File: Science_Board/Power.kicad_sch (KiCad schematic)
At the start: 29 parts, among them IC1 TCKE602RM, IC2 TCKE602RM, IC3 TCKE602RM, J21 Molex_Megafit_02, J3 Molex_Megafit_02, J4 Molex_Megafit_02, Q1 BS250, U1 AP63205WU

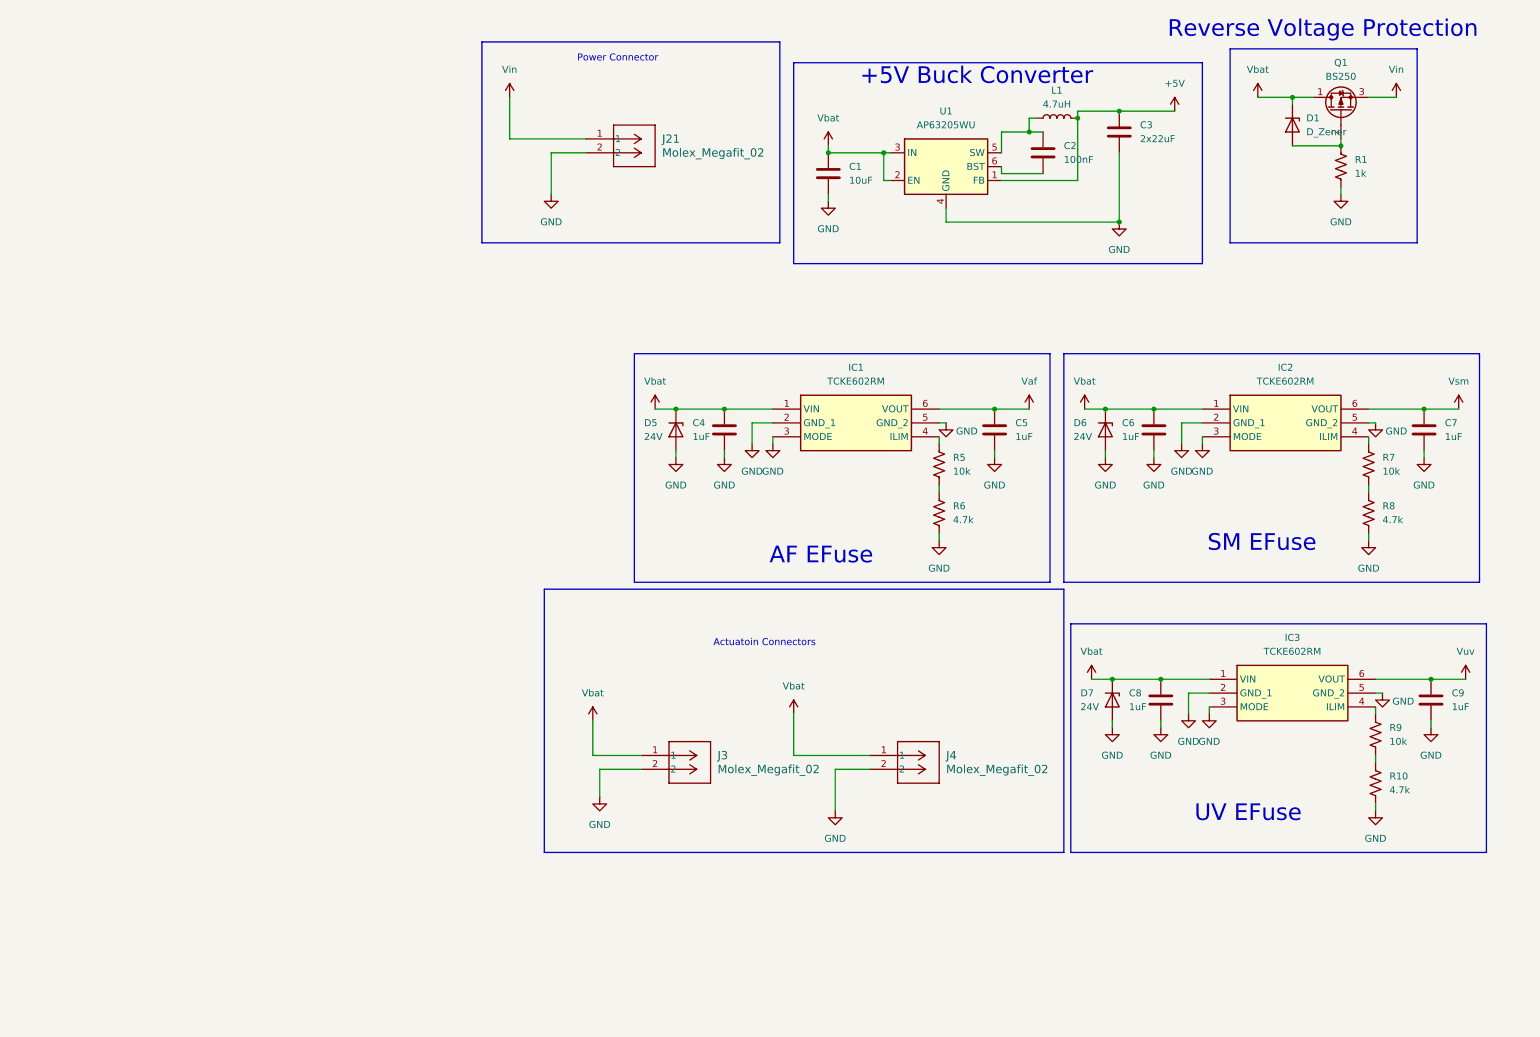
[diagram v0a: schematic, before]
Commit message: fuse trip
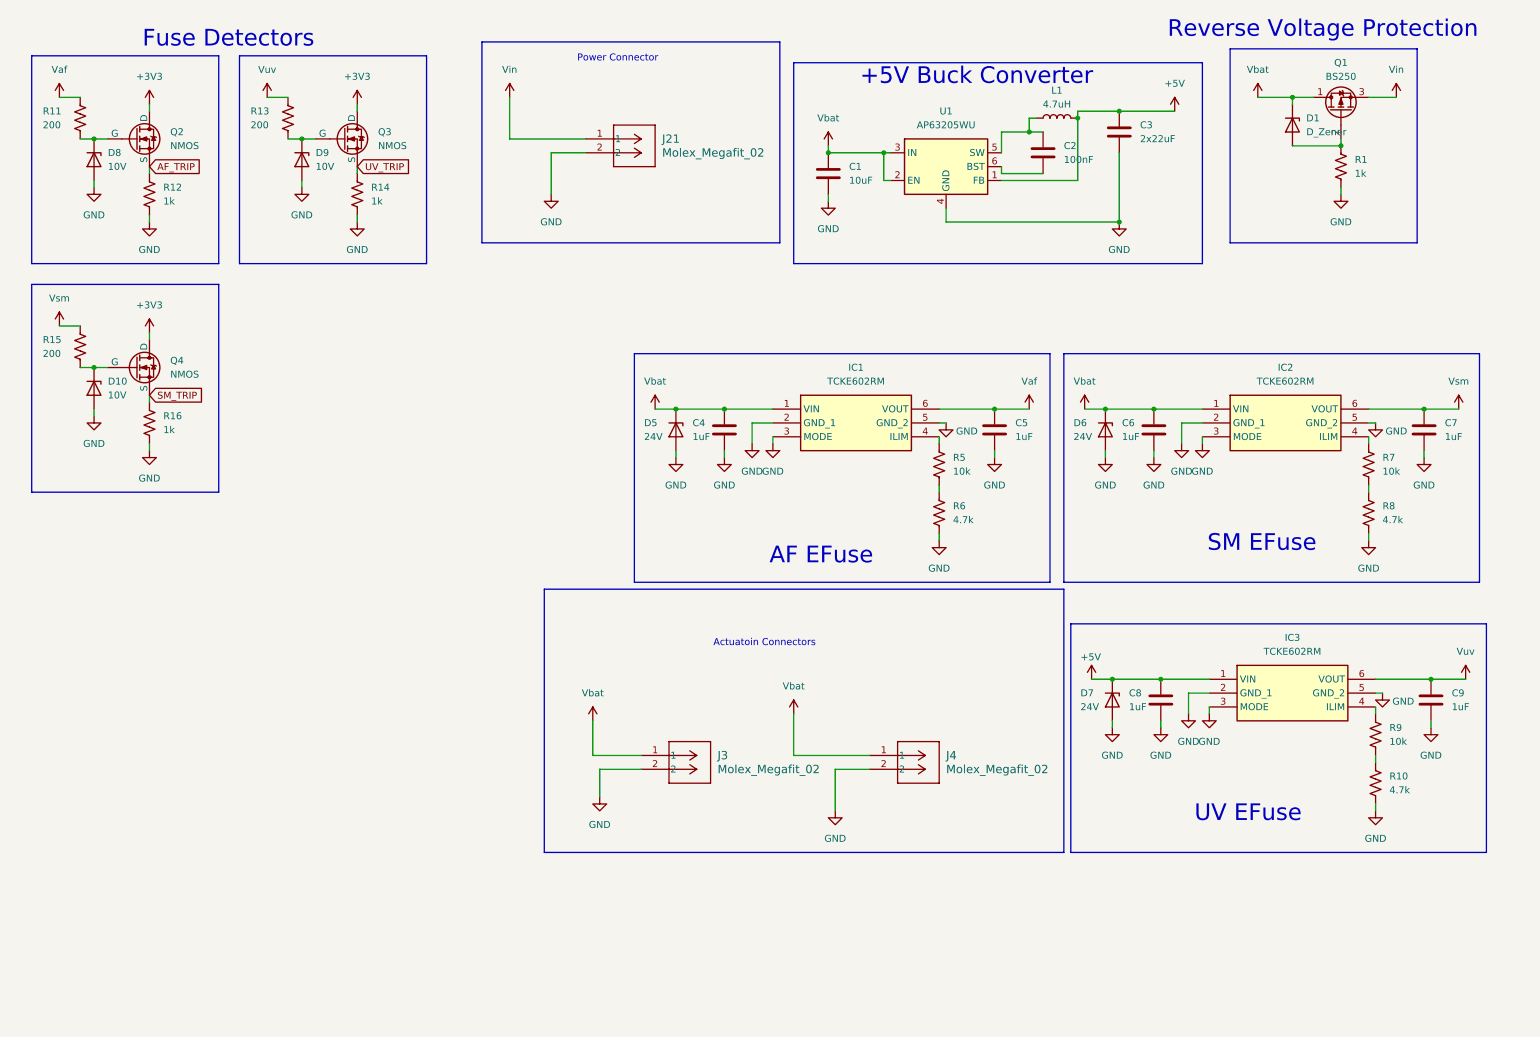
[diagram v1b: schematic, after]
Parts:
- added D10, D8, D9: 10V, Package_DIP:DIP-40_W15.24mm, symbol Device:D_Zener
- added Q2, Q3, Q4: NMOS, Package_DFN_QFN:Nordic_AQFN-94-1EP_7x7mm_P0.4mm, symbol Simulation_SPICE:NMOS
- added R11, R13, R15: 200, Resistor_SMD:R_0603_1608Metric_Pad0.98x0.95mm_HandSolder, symbol Device:R_US
- added R12, R14, R16: 1k, Resistor_SMD:R_0603_1608Metric_Pad0.98x0.95mm_HandSolder, symbol Device:R_US
- C4, C5, C6, C7, C8, C9: footprint (none) -> Capacitor_SMD:C_0603_1608Metric_Pad1.08x0.95mm_HandSolder
- IC1, IC2, IC3: footprint TCKE602RM -> MRDT_Devices:TCKE602RM
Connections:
- net +5V: now also C8.1, D7.1 (K), IC3.1 (VIN)
- net GND: now also D10.2 (A), D8.2 (A), D9.2 (A), R12.2, R14.2, R16.2
- net Vaf: now also R11.1
- net Vbat: no longer C8.1, D7.1 (K), IC3.1 (VIN)
- net Vsm: now also R15.1
- net Vuv: now also R13.1
- new net: D9.1 (K), Q3.2 (G), R13.2
- new net: D10.1 (K), Q4.2 (G), R15.2
- new net: D8.1 (K), Q2.2 (G), R11.2
- new net +3V3: Q2.1 (D), Q3.1 (D), Q4.1 (D)
- new net AF_TRIP: Q2.3 (S), R12.1
- new net SM_TRIP: Q4.3 (S), R16.1
- new net UV_TRIP: Q3.3 (S), R14.1
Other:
- note added: "Fuse Detectors"

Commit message: Add Footprints
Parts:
- R5, R7, R9: footprint (none) -> Resistor_SMD:R_0603_1608Metric
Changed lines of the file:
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@@
 			)
 		)
-		(property "Footprint" ""
+		(property "Footprint" "Resistor_SMD:R_0603_1608Metric"
 			(at 183.896 95.504 90)
 			(hide yes)
@@
 			)
 		)
-		(property "Footprint" ""
+		(property "Footprint" "Resistor_SMD:R_0603_1608Metric"
 			(at 262.636 95.504 90)
 			(hide yes)
@@
 			)
 		)
-		(property "Footprint" ""
+		(property "Footprint" "Resistor_SMD:R_0603_1608Metric"
 			(at 263.906 145.034 90)
 			(hide yes)

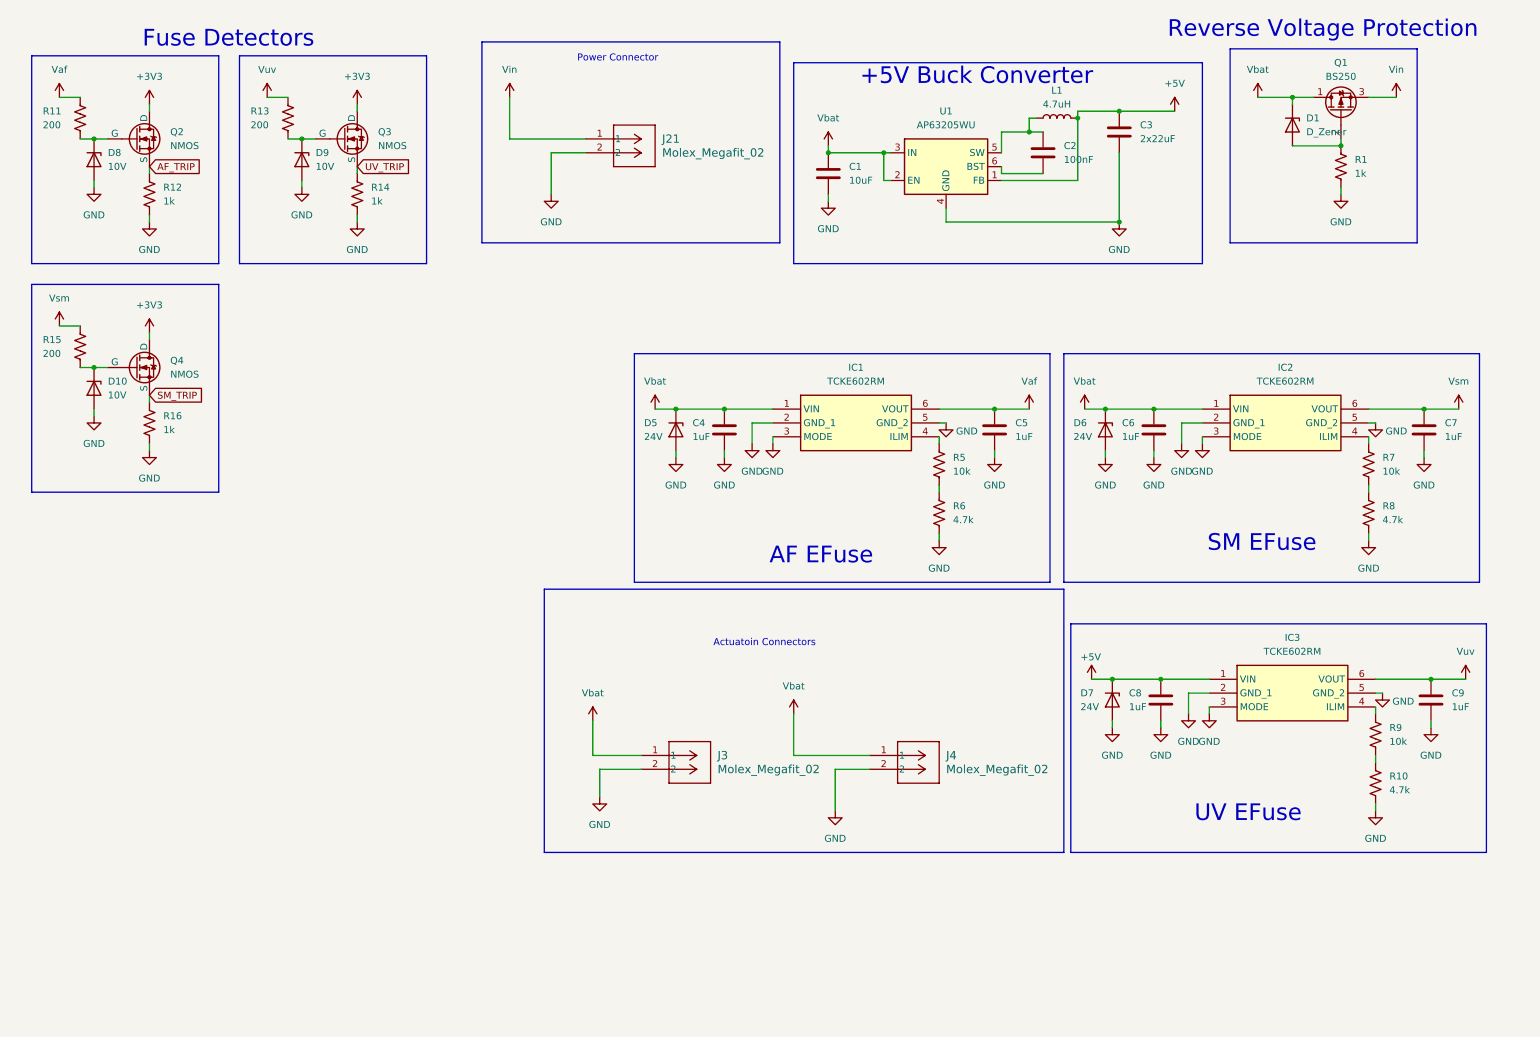
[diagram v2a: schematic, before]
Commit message: Fixed Reverse Voltage Protection, small formatting fixes
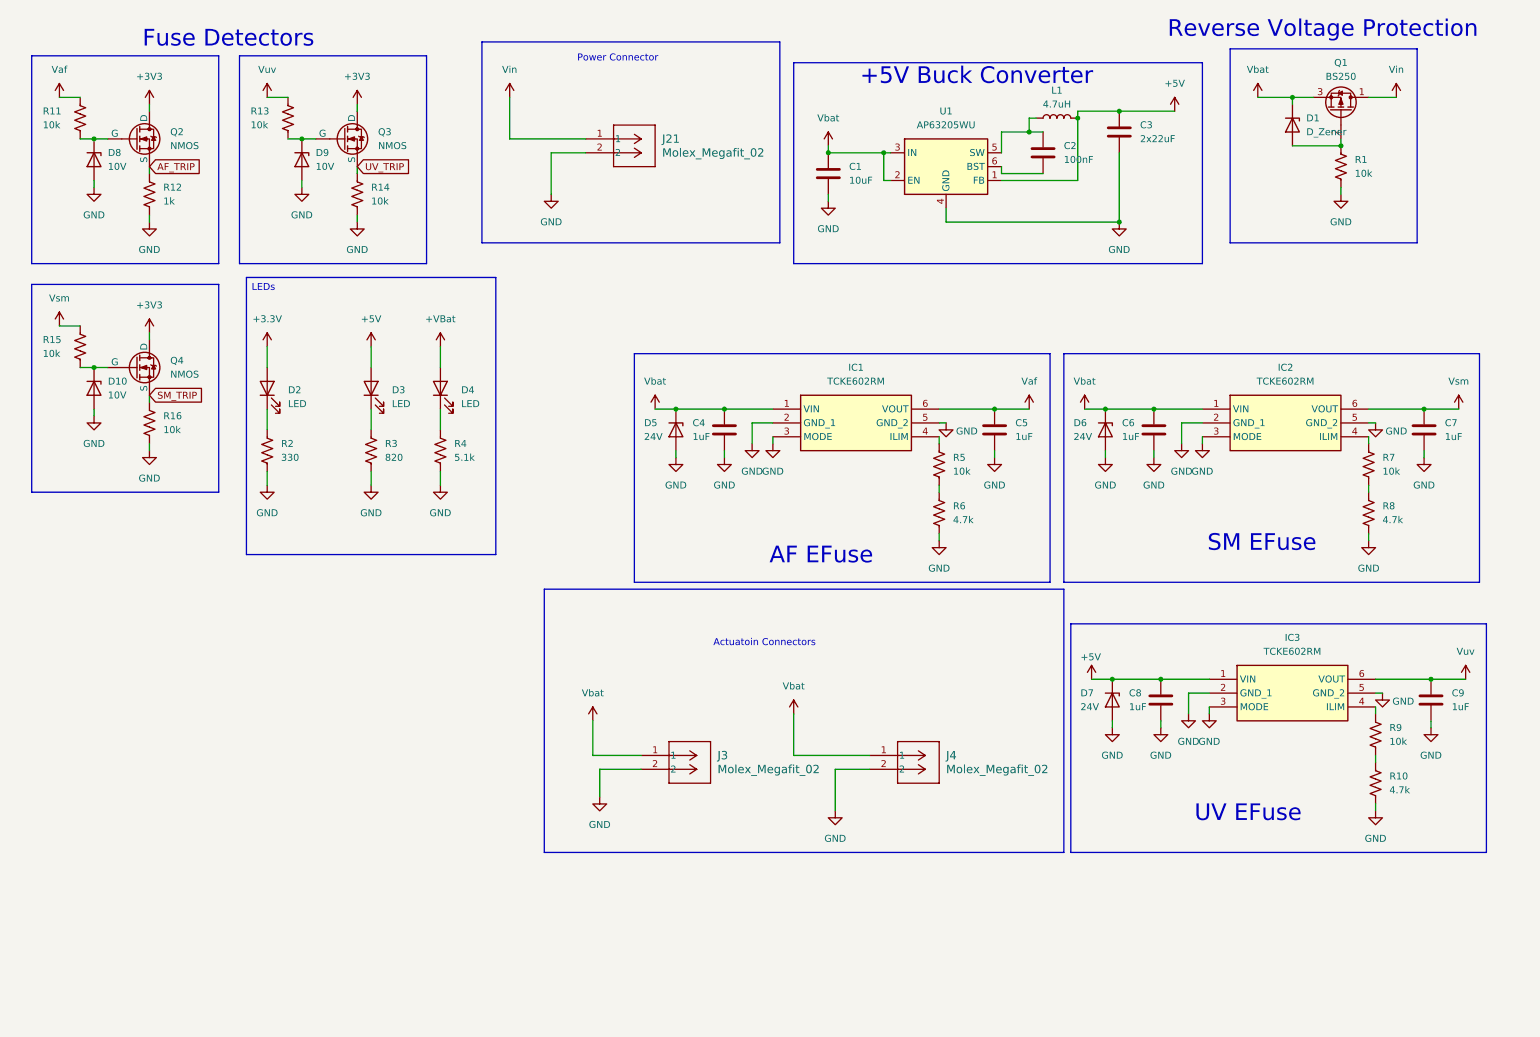
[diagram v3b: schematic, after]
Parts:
- added D2, D3, D4: LED, Diode_SMD:D_0603_1608Metric_Pad1.05x0.95mm_HandSolder, symbol Device:LED
- added R2: 330, Package_DIP:DIP-8_W7.62mm, symbol Device:R_US
- added R3: 820, Package_DIP:DIP-8_W7.62mm, symbol Device:R_US
- added R4: 5.1k, Package_DIP:DIP-8_W7.62mm, symbol Device:R_US
- R1, R14, R16: value 1k -> 10k
- R11, R13, R15: value 200 -> 10k
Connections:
- net +5V: now also D3.2 (A)
- net GND: now also R2.2, R3.2, R4.2
- net Vbat: now also Q1.3 (S); no longer Q1.1 (D)
- net Vin: now also Q1.1 (D); no longer Q1.3 (S)
- new net: D4.1 (K), R4.1
- new net: D3.1 (K), R3.1
- new net: D2.1 (K), R2.1
- new net +3.3V: D2.2 (A)
- new net +VBat: D4.2 (A)
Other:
- moved on the sheet: Q1

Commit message: Incorrect Efuse Package, fixed and added gpio connections for loadswitch functionality
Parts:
- IC1, IC2: value TCKE602RM -> TCKE603RA
- IC3: value TCKE602RM -> TCKE603RM
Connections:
- net GND: no longer IC1.3 (MODE), IC2.3 (MODE), IC3.3 (MODE)
- new net AF_EN: IC1.3 (EN)
- new net SM_EN: IC2.3 (EN)
- new net UV_EN: IC3.3 (EN)
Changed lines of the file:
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@@
 		)
 	)
+	(global_label "UV_EN"
+		(shape input)
+		(at 232.41 140.97 270)
+		(fields_autoplaced yes)
+		(effects
+			(font
+				(size 1.27 1.27)
+				(thickness 0.1588)
+			)
+			(justify right)
+		)
+		(property "Intersheetrefs" "${INTERSHEET_REFS}"
+			(at 232.41 149.8214 90)
+			(hide yes)
+			(show_name no)
+			(do_not_autoplace no)
+			(effects
+				(font
+					(size 1.27 1.27)
+				)
+				(justify right)
+			)
+		)
+	)
+	(global_label "AF_EN"
+		(shape input)
+		(at 152.4 91.44 270)
+		(fields_autoplaced yes)
+		(effects
+			(font
+				(size 1.27 1.27)
+				(thickness 0.1588)
+			)
+			(justify right)
+		)
+		(property "Intersheetrefs" "${INTERSHEET_REFS}"
+			(at 152.4 100.0495 90)
+			(hide yes)
+			(show_name no)
+			(do_not_autoplace no)
+			(effects
+				(font
+					(size 1.27 1.27)
+				)
+				(justify right)
+			)
+		)
+	)
+	(global_label "SM_EN"
+		(shape input)
+		(at 231.14 91.44 270)
+		(fields_autoplaced yes)
+		(effects
+			(font
+				(size 1.27 1.27)
+				(thickness 0.1588)
+			)
+			(justify right)
+		)
+		(property "Intersheetrefs" "${INTERSHEET_REFS}"
+			(at 231.14 100.5332 90)
+			(hide yes)
+			(show_name no)
+			(do_not_autoplace no)
+			(effects
+				(font
+					(size 1.27 1.27)
+				)
+				(justify right)
+			)
+		)
+	)
 	(global_label "AF_TRIP"
 		(shape input)
@@
 	)
 	(symbol
-		(lib_id "power:GND")
-		(at 232.41 140.97 0)
-		(unit 1)
-		(body_style 1)
-		(exclude_from_sim no)
-		(in_bom yes)
-		(on_board yes)
-		(in_pos_files yes)
-		(dnp no)
-		(fields_autoplaced yes)
-		(property "Reference" "#PWR038"
-			(at 232.41 147.32 0)
-			(hide yes)
-			(show_name no)
-			(do_not_autoplace no)
-			(effects
-				(font
-					(size 1.27 1.27)
-				)
-			)
-		)
-		(property "Value" "GND"
-			(at 232.41 146.05 0)
-			(show_name no)
-			(do_not_autoplace no)
-			(effects
-				(font
-					(size 1.27 1.27)
-				)
-			)
-		)
-		(property "Footprint" ""
-			(at 232.41 140.97 0)
-			(hide yes)
-			(show_name no)
-			(do_not_autoplace no)
-			(effects
-				(font
-					(size 1.27 1.27)
-				)
-			)
-		)
-		(property "Datasheet" ""
-			(at 232.41 140.97 0)
-			(hide yes)
-			(show_name no)
-			(do_not_autoplace no)
-			(effects
-				(font
-					(size 1.27 1.27)
-				)
-			)
-		)
-		(property "Description" "Power symbol creates a global label with name \"GND\" , ground"
-			(at 232.41 140.97 0)
-			(hide yes)
-			(show_name no)
-			(do_not_autoplace no)
-			(effects
-				(font
-					(size 1.27 1.27)
-				)
-			)
-		)
-		(pin "1"
-		)
-		(instances
-			(project "Science_Board"
-				(path "/4f5c5f7f-4385-4de2-96ca-2ae741ebf691/6219bf49-5574-4710-86f4-9f93da84ad76"
-					(reference "#PWR038")
-					(unit 1)
-				)
-			)
-		)
-	)
-	(symbol
 		(lib_id "Device:C")
 		(at 193.04 88.9 0)
@@
 	)
 	(symbol
+		(lib_name "TCKE602RM_1")
 		(lib_id "MRDT_TCKE602RM:TCKE602RM")
 		(at 231.14 85.09 0)
@@
 			)
 		)
-		(property "Value" "TCKE602RM"
+		(property "Value" "TCKE603RA"
 			(at 246.38 80.01 0)
 			(show_name no)
@@
 	)
 	(symbol
-		(lib_id "power:GND")
-		(at 231.14 91.44 0)
-		(unit 1)
-		(body_style 1)
-		(exclude_from_sim no)
-		(in_bom yes)
-		(on_board yes)
-		(in_pos_files yes)
-		(dnp no)
-		(fields_autoplaced yes)
-		(property "Reference" "#PWR029"
-			(at 231.14 97.79 0)
-			(hide yes)
-			(show_name no)
-			(do_not_autoplace no)
-			(effects
-				(font
-					(size 1.27 1.27)
-				)
-			)
-		)
-		(property "Value" "GND"
-			(at 231.14 96.52 0)
-			(show_name no)
-			(do_not_autoplace no)
-			(effects
-				(font
-					(size 1.27 1.27)
-				)
-			)
-		)
-		(property "Footprint" ""
-			(at 231.14 91.44 0)
-			(hide yes)
-			(show_name no)
-			(do_not_autoplace no)
-			(effects
-				(font
-					(size 1.27 1.27)
-				)
-			)
-		)
-		(property "Datasheet" ""
-			(at 231.14 91.44 0)
-			(hide yes)
-			(show_name no)
-			(do_not_autoplace no)
-			(effects
-				(font
-					(size 1.27 1.27)
-				)
-			)
-		)
-		(property "Description" "Power symbol creates a global label with name \"GND\" , ground"
-			(at 231.14 91.44 0)
-			(hide yes)
-			(show_name no)
-			(do_not_autoplace no)
-			(effects
-				(font
-					(size 1.27 1.27)
-				)
-			)
-		)
-		(pin "1"
-		)
-		(instances
-			(project "Science_Board"
-				(path "/4f5c5f7f-4385-4de2-96ca-2ae741ebf691/6219bf49-5574-4710-86f4-9f93da84ad76"
-					(reference "#PWR029")
-					(unit 1)
-				)
-			)
-		)
-	)
-	(symbol
 		(lib_id "power:VCC")
 		(at 279.4 134.62 0)
@@
 	)
 	(symbol
-		(lib_id "power:GND")
-		(at 152.4 91.44 0)
-		(unit 1)
-		(body_style 1)
-		(exclude_from_sim no)
-		(in_bom yes)
-		(on_board yes)
-		(in_pos_files yes)
-		(dnp no)
-		(fields_autoplaced yes)
-		(property "Reference" "#PWR017"
-			(at 152.4 97.79 0)
-			(hide yes)
-			(show_name no)
-			(do_not_autoplace no)
-			(effects
-				(font
-					(size 1.27 1.27)
-				)
-			)
-		)
-		(property "Value" "GND"
-			(at 152.4 96.52 0)
-			(show_name no)
-			(do_not_autoplace no)
-			(effects
-				(font
-					(size 1.27 1.27)
-				)
-			)
-		)
-		(property "Footprint" ""
-			(at 152.4 91.44 0)
-			(hide yes)
-			(show_name no)
-			(do_not_autoplace no)
-			(effects
-				(font
-					(size 1.27 1.27)
-				)
-			)
-		)
-		(property "Datasheet" ""
-			(at 152.4 91.44 0)
-			(hide yes)
-			(show_name no)
-			(do_not_autoplace no)
-			(effects
-				(font
-					(size 1.27 1.27)
-				)
-			)
-		)
-		(property "Description" "Power symbol creates a global label with name \"GND\" , ground"
-			(at 152.4 91.44 0)
-			(hide yes)
-			(show_name no)
-			(do_not_autoplace no)
-			(effects
-				(font
-					(size 1.27 1.27)
-				)
-			)
-		)
-		(pin "1"
-		)
-		(instances
-			(project "Science_Board"
-				(path "/4f5c5f7f-4385-4de2-96ca-2ae741ebf691/6219bf49-5574-4710-86f4-9f93da84ad76"
-					(reference "#PWR017")
-					(unit 1)
-				)
-			)
-		)
-	)
-	(symbol
 		(lib_id "Device:R_US")
 		(at 78.74 92.71 0)
@@
 			)
 		)
-		(property "Value" "TCKE602RM"
+		(property "Value" "TCKE603RA"
 			(at 167.64 80.01 0)
 			(show_name no)
@@
 	)
 	(symbol
+		(lib_name "TCKE602RM_2")
 		(lib_id "MRDT_TCKE602RM:TCKE602RM")
 		(at 232.41 134.62 0)
@@
 			)
 		)
-		(property "Value" "TCKE602RM"
+		(property "Value" "TCKE603RM"
 			(at 247.65 129.54 0)
 			(show_name no)

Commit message: fixed some mistakes like making a box for buttons and the voltage flag being wrong for PWM driver
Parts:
- added C11: 22uF, Package_SO:SOIC-8_3.9x4.9mm_P1.27mm, symbol Device:C
- C3: value 2x22uF -> 22uF
- D2, D3, D4: value LED -> GREEN LED
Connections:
- net GND: now also C11.2; no longer C3.2
- new net: C11.1, C3.2
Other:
- moved on the sheet: C7

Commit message: created decoupling capacitors
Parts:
- added C12: 0.1uF, symbol Device:C
- added C13: 10uf, symbol Device:C
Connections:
- net GND: now also C12.2, C13.1
- net Vbat: now also C12.1, C13.2
